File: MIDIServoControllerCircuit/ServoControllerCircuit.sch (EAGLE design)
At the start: 26 parts, among them Q1 20MHz, T1 2N3904, X1 SIGNAL-PWR-GND, X2 SIGNAL-PWR-GND

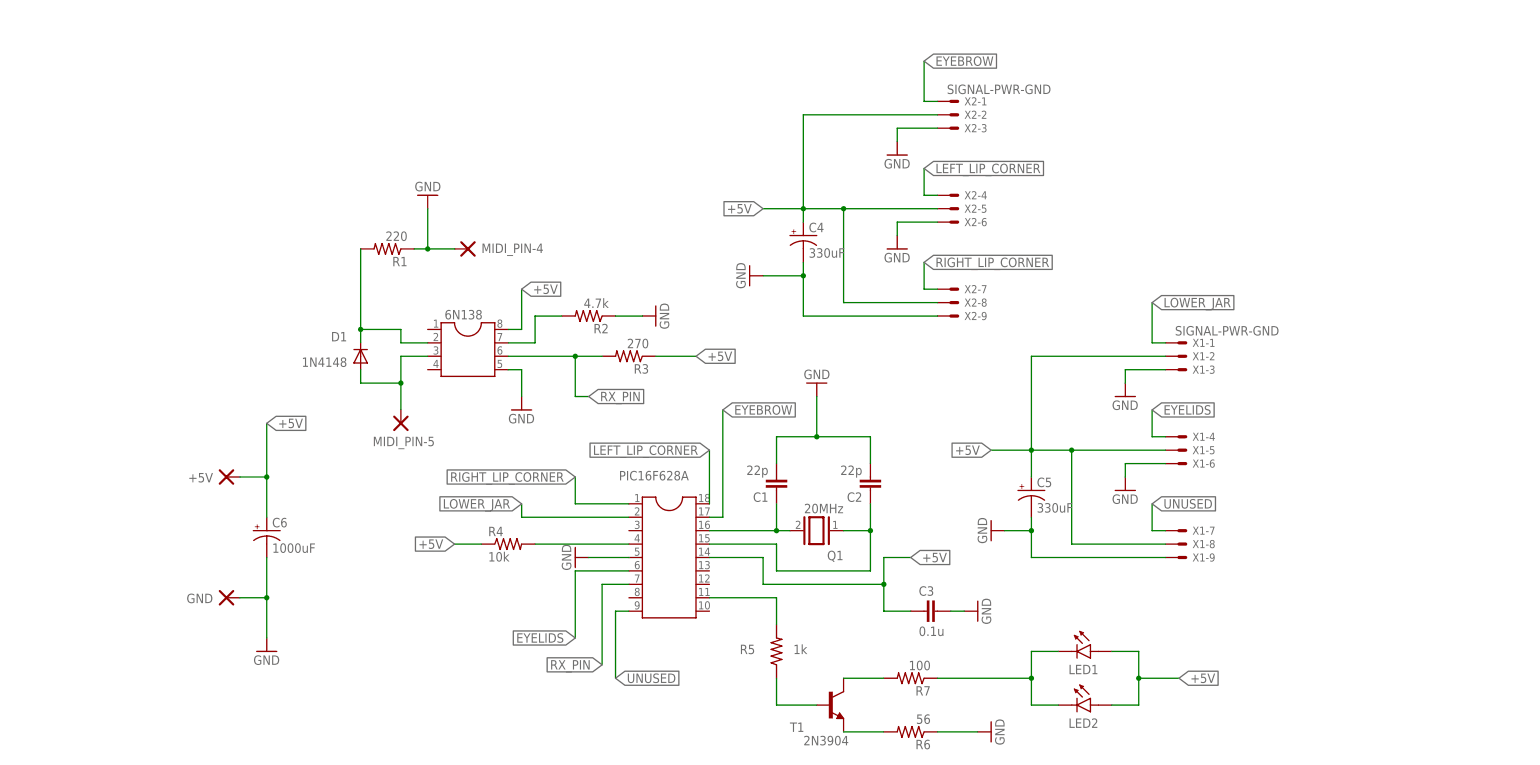
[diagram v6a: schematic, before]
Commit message: Updated Circuit for better PIC to compensate for more motor control.
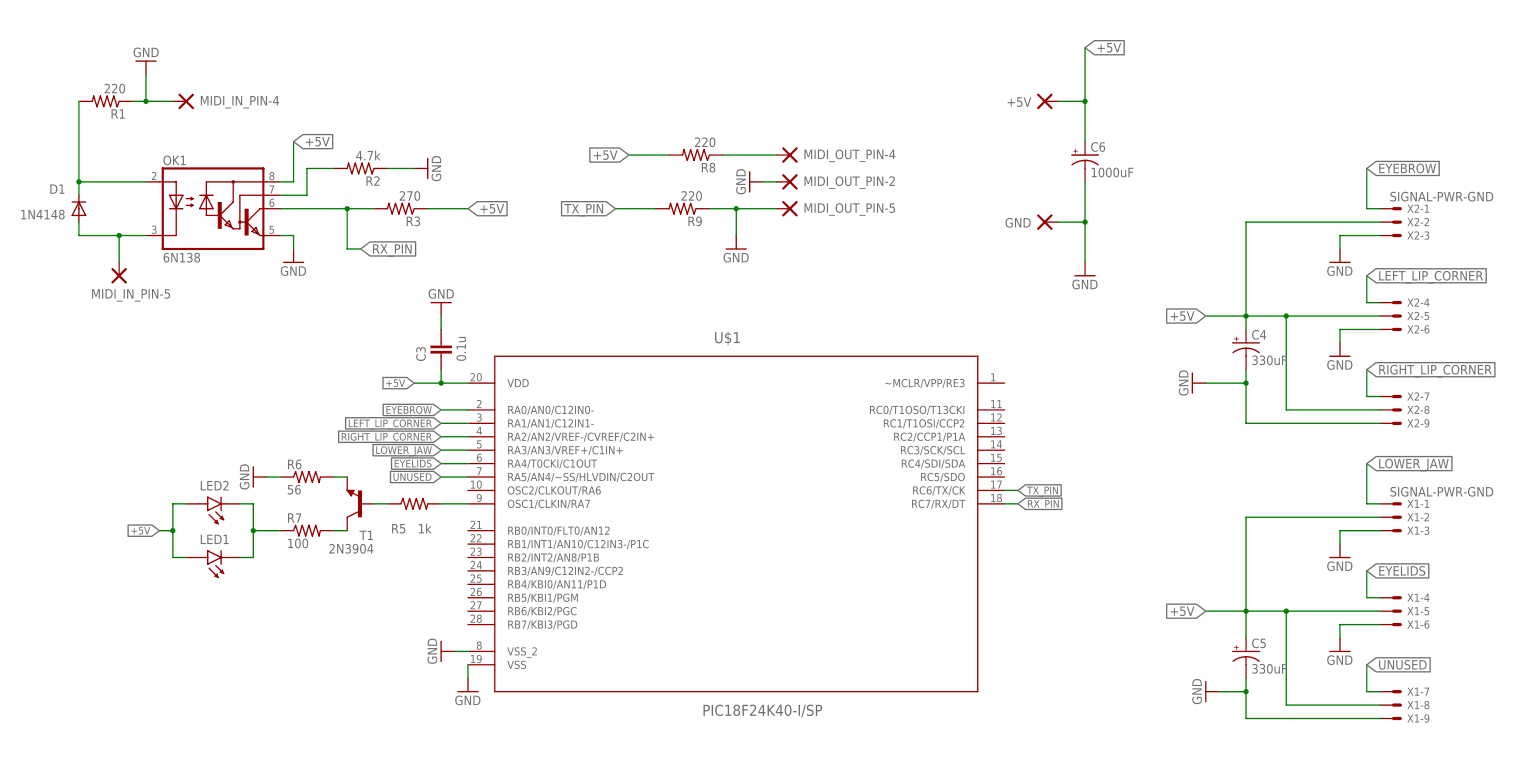
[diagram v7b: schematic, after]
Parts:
- removed 6N138: (no value), ic-package:DIL8S
- removed C1, C2: 22p, resistor:C-EU050-025X075
- removed MIDI_PIN-4, MIDI_PIN-5: DOUBLE_THROUGH_HOLE_PAD, DOUBLE_THROUGH_HOLE_PAD:DOUBLE_THROUGH_HOLE_PAD
- removed PIC16F628A: (no value), ic-package:DIL18S
- removed Q1: 20MHz, special:XTAL/S
- removed R4: 10k, resistor:R-US_0207/12
- added MIDI_IN_PIN-4, MIDI_IN_PIN-5, MIDI_OUT_PIN-2, MIDI_OUT_PIN-4, MIDI_OUT_PIN-5: DOUBLE_THROUGH_HOLE_PAD, DOUBLE_THROUGH_HOLE_PAD:DOUBLE_THROUGH_HOLE_PAD
- added OK1: 6N138, optocoupler:6N138
- added R8, R9: 220, resistor:R-US_0207/12
- added U$1: PIC18F24K40-I/SP, Microchip_By_element14_Batch_1:PIC18F24K20-I/SP
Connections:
- removed net LOWER_JAR: PIC16F628A.2, X1-1.S
- removed net N$3: C1.1, PIC16F628A.16, Q1.2
- removed net N$4: C2.1, PIC16F628A.15, Q1.1
- removed net N$6: PIC16F628A.4, R4.2
- new net LOWER_JAW: U$1.RA3/AN3/VREF+/C1IN+, X1-1.S
- new net N$11: MIDI_OUT_PIN-4.P$1, R8.1
- new net TX_PIN: R9.2, U$1.RC6/TX/CK
- net +5V: now also OK1.VCC, R8.2, U$1.VDD; no longer 6N138.8, PIC16F628A.14, R4.1
- net EYEBROW: now also U$1.RA0/AN0/C12IN0-; no longer PIC16F628A.17
- net EYELIDS: now also U$1.RA4/T0CKI/C1OUT; no longer PIC16F628A.6
- net GND: now also MIDI_IN_PIN-4.P$1, MIDI_OUT_PIN-2.P$1, MIDI_OUT_PIN-5.P$1, OK1.GND, R9.1, U$1.VSS, U$1.VSS_2; no longer 6N138.5, C1.2, C2.2, MIDI_PIN-4.P$1, PIC16F628A.5
- net LEFT_LIP_CORNER: now also U$1.RA1/AN1/C12IN1-; no longer PIC16F628A.18
- net LIGHTS: now also U$1.OSC1/CLKIN/RA7; no longer PIC16F628A.11
- net MIDI_PIN-5: now also MIDI_IN_PIN-5.P$1, OK1.C; no longer 6N138.3, MIDI_PIN-5.P$1
- net N$1: now also OK1.A; no longer 6N138.2
- net N$2: now also OK1.VB; no longer 6N138.7
- net RIGHT_LIP_CORNER: now also U$1.RA2/AN2/VREF-/CVREF/C2IN+; no longer PIC16F628A.1
- net RX_PIN: now also OK1.VO, U$1.RC7/RX/DT; no longer 6N138.6, PIC16F628A.7
- net UNUSED: now also U$1.RA5/AN4/~SS/HLVDIN/C2OUT; no longer PIC16F628A.9
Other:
- moved on the sheet: +5V, C3, C4, C5, C6, D1, GND, LED1, LED2, R1, R2, R3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

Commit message: Took MIDI output and input circuits out, replaced with XBee circuit. Cleaned up schematic.
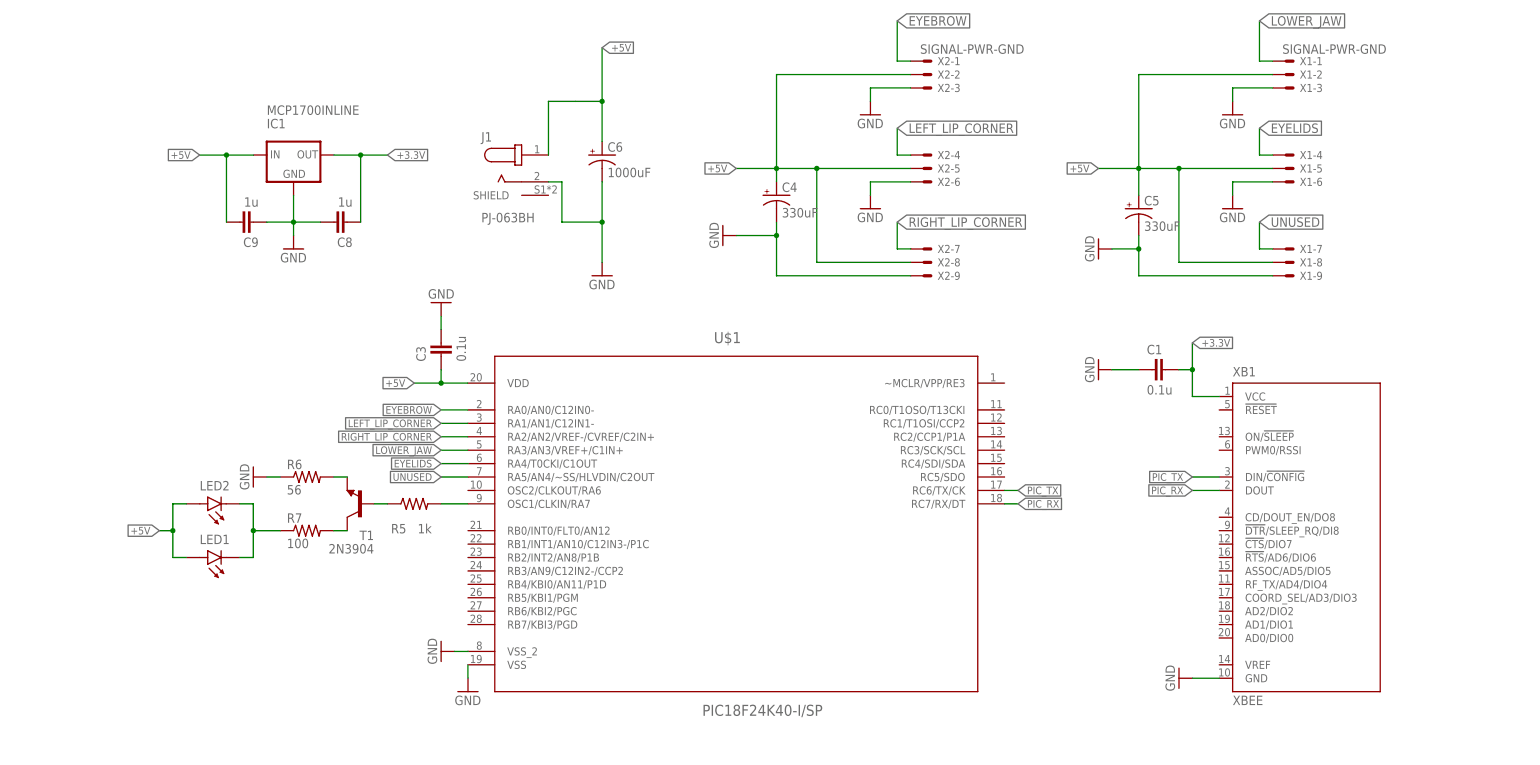
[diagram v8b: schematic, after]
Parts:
- removed +5V, GND, MIDI_IN_PIN-4, MIDI_IN_PIN-5, MIDI_OUT_PIN-2, MIDI_OUT_PIN-4, MIDI_OUT_PIN-5: DOUBLE_THROUGH_HOLE_PAD, DOUBLE_THROUGH_HOLE_PAD:DOUBLE_THROUGH_HOLE_PAD
- removed D1: 1N4148, diode:1N4148DO35-10
- removed OK1: 6N138, optocoupler:6N138
- removed R1, R8, R9: 220, resistor:R-US_0207/12
- removed R2: 4.7k, resistor:R-US_0207/12
- removed R3: 270, resistor:R-US_0207/12
- added C1: 0.1u, resistor:C-EU050-025X075
- added C8, C9: 1u, resistor:C-EU050-025X075
- added IC1: MCP1700INLINE, MCP1700:MCP1700INLINE
- added J1: PJ-063BH, PJ-063BH:PJ-063BH
- added XB1: XBEE, maxstream:XBEE
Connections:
- removed net MIDI_PIN-5: D1.A, MIDI_IN_PIN-5.P$1, OK1.C
- removed net N$1: D1.C, OK1.A, R1.2
- removed net N$11: MIDI_OUT_PIN-4.P$1, R8.1
- removed net N$2: OK1.VB, R2.2
- removed net RX_PIN: OK1.VO, R3.2, U$1.RC7/RX/DT
- removed net TX_PIN: R9.2, U$1.RC6/TX/CK
- new net +3.3V: C1.1, C8.2, IC1.OUT, XB1.VCC
- new net PIC_RX: U$1.RC7/RX/DT, XB1.DOUT
- new net PIC_TX: U$1.RC6/TX/CK, XB1.DIN/!CONFIG
- net +5V: now also C9.1, IC1.IN, J1.1; no longer +5V.P$1, OK1.VCC, R3.1, R8.2
- net GND: now also C1.2, C8.1, C9.2, IC1.GND, J1.2, XB1.GND; no longer GND.P$1, MIDI_IN_PIN-4.P$1, MIDI_OUT_PIN-2.P$1, MIDI_OUT_PIN-5.P$1, OK1.GND, R1.1, R2.1, R9.1
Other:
- moved on the sheet: C4, C5, C6, X1-1, X1-2, X1-3, X1-4, X1-5, X1-6, X1-7, X1-8, X1-9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
